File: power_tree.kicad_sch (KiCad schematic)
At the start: 16 parts, among them J2 BAT1_01x02_Pin, Q1 FDN340P, U3 TP4056-42-ESOP8, U4 AP2112K-3.3

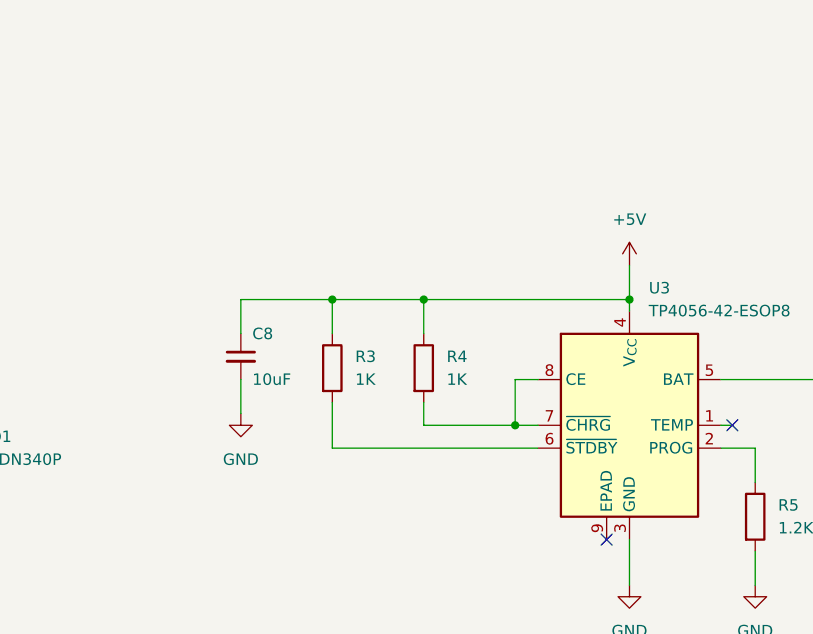
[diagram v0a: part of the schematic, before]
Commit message: fix(charger): split CE from CHRG status output
TP4056 CHRG pin was shorted to CE enable input, letting the
open-drain status output fight the R4 pull-up and risk disabling
charging. CE stays on R4 to +5V, CHRG moves to its own 1K pull-up
(R11) mirroring the STDBY network.
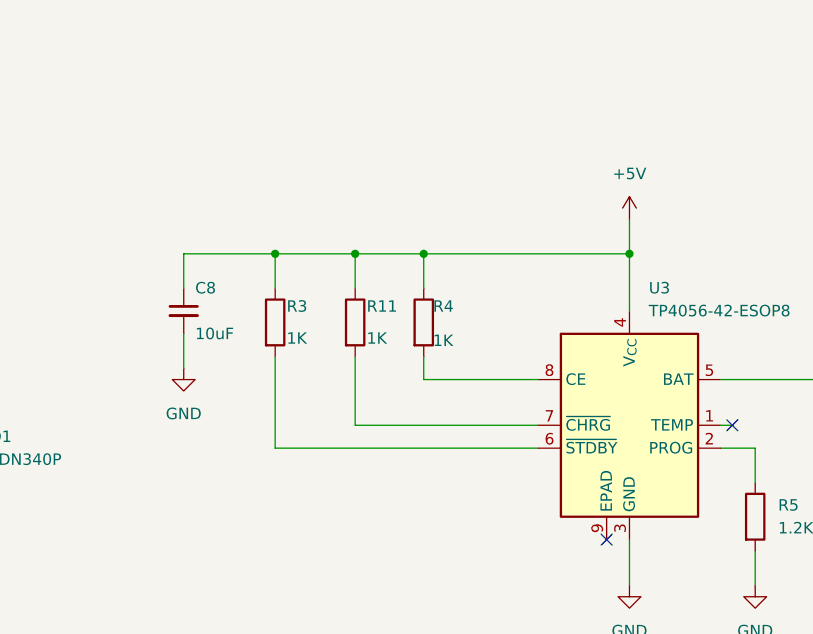
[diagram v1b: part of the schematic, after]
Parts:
- added R11: 1K, Resistor_SMD:R_0603_1608Metric_Pad0.98x0.95mm_HandSolder, symbol Device:R
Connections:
- net +5V: now also R11.1
- net at R4.2, U3.8 (CE): no longer U3.7 (~{CHRG})
- new net: R11.2, U3.7 (~{CHRG})
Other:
- moved on the sheet: C8, R3, R4

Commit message: fix(charger): tie TEMP to GND for no-NTC operation
TP4056 TEMP pin was floating, risking false over-temperature
suspend of charging. With no thermistor fitted, TEMP goes
directly to GND per datasheet.
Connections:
- net GND: now also U3.1 (TEMP)
- no-connect marks 2 -> 1
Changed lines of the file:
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@@
-	)
-	(no_connect
-		(at 133.35 102.87)
 	)
 	(no_connect
@@
 	(wire
 		(pts
+			(xy 143.51 102.87) (xy 143.51 120.65)
+		)
+		(stroke
+			(width 0)
+			(type default)
+		)
+	)
+	(wire
+		(pts
 			(xy 121.92 115.57) (xy 121.92 120.65)
 		)
@@
 	(wire
 		(pts
-			(xy 132.08 102.87) (xy 133.35 102.87)
+			(xy 132.08 102.87) (xy 143.51 102.87)
 		)
 		(stroke
@@
 					(unit 1)
 				)
+			)
+		)
+	)
+	(symbol
+		(lib_id "power:GND")
+		(at 143.51 120.65 0)
+		(unit 1)
+		(body_style 1)
+		(exclude_from_sim no)
+		(in_bom yes)
+		(on_board yes)
+		(in_pos_files yes)
+		(dnp no)
+		(fields_autoplaced yes)
+		(property "Reference" "#PWR065"
+			(at 143.51 127 0)
+			(hide yes)
+			(show_name no)
+			(do_not_autoplace no)
+			(effects
+				(font
+					(size 1.27 1.27)
+				)
+			)
+		)
+		(property "Value" "GND"
+			(at 143.51 125.73 0)
+			(show_name no)
+			(do_not_autoplace no)
+			(effects
+				(font
+					(size 1.27 1.27)
+				)
+			)
+		)
+		(property "Footprint" ""
+			(at 143.51 120.65 0)
+			(hide yes)
+			(show_name no)
+			(do_not_autoplace no)
+			(effects
+				(font
+					(size 1.27 1.27)
+				)
+			)
+		)
+		(property "Datasheet" ""
+			(at 143.51 120.65 0)
+			(hide yes)
+			(show_name no)
+			(do_not_autoplace no)
+			(effects
+				(font
+					(size 1.27 1.27)
+				)
+			)
+		)
+		(property "Description" "Power symbol creates a global label with name \"GND\" , ground"
+			(at 143.51 120.65 0)
+			(hide yes)
+			(show_name no)
+			(do_not_autoplace no)
+			(effects
+				(font
+					(size 1.27 1.27)
+				)
+			)
+		)
+		(pin "1"
+		)
+		(instances
+			(project "HW"
+				(path "/01550cd7-b424-469c-925b-c370f3609cd4/360b299b-84d8-4d26-8110-4c6e53cc9fa4"
+					(reference "#PWR065")
+					(unit 1)
+				)
